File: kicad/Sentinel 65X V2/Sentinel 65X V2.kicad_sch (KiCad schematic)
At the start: 158 parts, among them J1 SNES Controller, J10 Conn_02x15_Counter_Clockwise, J11 Conn_01x02, J12 Conn_01x02, J13 LEFT, J14 RIGHT, J15 USB_C_Receptacle_PowerOnly_6P, J2 SNES Controller, J4 JTAG Header, J5 2x32 2.54mm Card Edge Connect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

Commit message: Updated pinouts
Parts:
- removed J10: Conn_02x15_Counter_Clockwise, symbol Sentinel 65X V2:Conn_02x15_Counter_Clockwise
- removed R81: 3.3kΩ, Resistor_SMD:R_0402_1005Metric, symbol Sentinel 65X V2:R
- added J10: FPGA Flash Prog, symbol Connector_Generic:Conn_02x04_Odd_Even
- added J3: Conn_02x12_Odd_Even, symbol Connector_Generic:Conn_02x12_Odd_Even
- added R44, R52, R60, R61: 10kΩ, Resistor_SMD:R_0402_1005Metric, symbol Sentinel 65X V2:R
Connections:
- net +3.3V: now also J3.2 (Pin_2), R44.1, R52.1, R60.1
- net A0: now also J3.16 (Pin_16)
- net A1: now also J3.15 (Pin_15)
- net A2: now also J3.14 (Pin_14)
- net A3: now also J3.13 (Pin_13)
- net CDONE: now also J10.1 (Pin_1)
- net D0: now also J3.24 (Pin_24)
- net D1: now also J3.23 (Pin_23)
- net D2: now also J3.22 (Pin_22)
- net D3: now also J3.21 (Pin_21)
- net D4: now also J3.20 (Pin_20)
- net D5: now also J3.19 (Pin_19)
- net D6: now also J3.18 (Pin_18)
- net D7: now also J3.17 (Pin_17)
- net FPGA_MISO: now also J10.6 (Pin_6), R60.2
- net FPGA_MOSI: now also J10.5 (Pin_5), R52.2
- net FPGA_SCK: now also J10.4 (Pin_4), R61.1
- net GND: now also J10.7 (Pin_7), J10.8 (Pin_8), J3.1 (Pin_1), R61.2
- net I2C_SCL: now also J3.4 (Pin_4)
- net I2C_SDA: now also J3.6 (Pin_6)
- net PHI2: now also J3.9 (Pin_9)
- net RXD: now also J3.5 (Pin_5)
- net TXD: now also J3.3 (Pin_3)
- net ~{CLOCK}: now also J3.10 (Pin_10)
- net ~{FLASH_SS}: now also J10.2 (Pin_2)
- net ~{FPGA_RES}: now also J10.3 (Pin_3), R44.2
- net ~{IRQ}2: now also J3.8 (Pin_8)
- net ~{RD}: now also J3.11 (Pin_11)
- net ~{RES}: now also J3.7 (Pin_7)
- net ~{WR}: now also J3.12 (Pin_12)
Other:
- moved on the sheet: R21, R70, R71

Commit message: Updated schematic to add RTS/CTS flow control to debug UART (required by CPU's on-chip ROM monitor)
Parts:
- removed J3: Conn_02x12_Odd_Even, symbol Connector_Generic:Conn_02x12_Odd_Even
- removed R38, R46, R70, R71: 3.3kΩ, Resistor_SMD:R_0402_1005Metric, symbol Sentinel 65X V2:R
- added D9: LED, symbol Sentinel 65X V2:LED
- added J3: Conn_02x13_Counter_Clockwise, symbol Connector_Generic:Conn_02x13_Counter_Clockwise
- R35: value 3.3kΩ -> 1kΩ
- U2: footprint Package_LCC:PLCC-84_SMD-Socket -> Package_LCC:PLCC-84_THT-Socket
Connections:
- net +3.3V: now also J3.26 (Pin_26); no longer R35.1
- net A0: now also J3.18 (Pin_18)
- net A1: now also J3.9 (Pin_9)
- net A2: now also J3.19 (Pin_19)
- net A3: now also J3.8 (Pin_8)
- net BL0: now also U2.4 (P60); no longer U2.77 (P47)
- net BL1: now also U2.5 (P61); no longer U2.76 (P46)
- net CDONE: now also R35.2; no longer R41.2
- net D0: now also J3.14 (Pin_14)
- net D1: now also J3.13 (Pin_13)
- net D2: now also J3.15 (Pin_15)
- net D3: now also J3.12 (Pin_12)
- net D4: now also J3.16 (Pin_16)
- net D5: now also J3.11 (Pin_11)
- net D6: now also J3.17 (Pin_17)
- net D7: now also J3.10 (Pin_10)
- net GND: now also D9.1 (K), J3.1 (Pin_1)
- net I2C_SCL: now also U2.77 (P47), J3.25 (Pin_25); no longer U2.11 (P67)
- net I2C_SDA: now also U2.76 (P46), J3.24 (Pin_24); no longer U2.9 (P65)
- net PHI2: now also J3.6 (Pin_6)
- net RXD: now also U2.9 (P65), J3.3 (Pin_3); no longer U2.6 (P62)
- net TXD: now also U2.11 (P67), J3.2 (Pin_2); no longer U2.5 (P61)
- net ~{CLOCK}: now also J3.21 (Pin_21)
- net ~{NMI}: now also J5.a26 (Pin_a26); no longer J5.b26 (Pin_b26)
- net ~{RD}: now also J3.7 (Pin_7)
- net ~{RES}: now also J3.23 (Pin_23)
- net ~{WR}: now also J3.20 (Pin_20)
- net IRQ3: no longer names the net of U4.5 (I/O/PD1)
- net IRQ3: no longer U2.4 (PE60)
- removed net VIRQ: J5.a26 (Pin_a26), U2.2 (PE56), U9.3 (IOB_9b)
- net ~{IRQ}0 renamed ~{IRQ}
- net ~{IRQ}: now also J3.22 (Pin_22)
- net ~{IRQ}2 renamed ~{VIRQ}
- net ~{VIRQ}: now also J5.a25 (Pin_a25), U2.8 (~{NE64}), U9.3 (IOB_9b); no longer U2.3 (~{NE57})
- removed net ~{IRQ}3: J5.b24 (Pin_b24), R35.2, U4.35 (I/O/GCLK3)
- net ~{IRQ}4: no longer names the net of J5.b25 (Pin_b25)
- net ~{IRQ}4: no longer U2.8 (~{NE64})
- removed net ~{IRQ}5: J5.a25 (Pin_a25), U2.10 (~{NE66})
- new net: D9.2 (A), R35.1
- new net BL2: R41.2, U2.6 (P62)
- new net CTS: J3.4 (Pin_4), U2.3 (P57)
- new net RTS: J3.5 (Pin_5), U2.2 (P56)
- no-connect marks 26 -> 31
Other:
- note added: "Clock OTP ROM Defaults: CLK: 32.768KHz TOD clock FCLK: 4MHz fast clock SYSCLK: 25MHz VERA clock"
- note removed: "Clock Defaults: CLK: 32.768KHz TOD clock FCLK: 8MHz+ fast clock SYSCLK: 25MHz VERA clock"
- moved on the sheet: D3, D4, D8, H1, H2, H3, H4, H5, H6, J12, J7, R23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

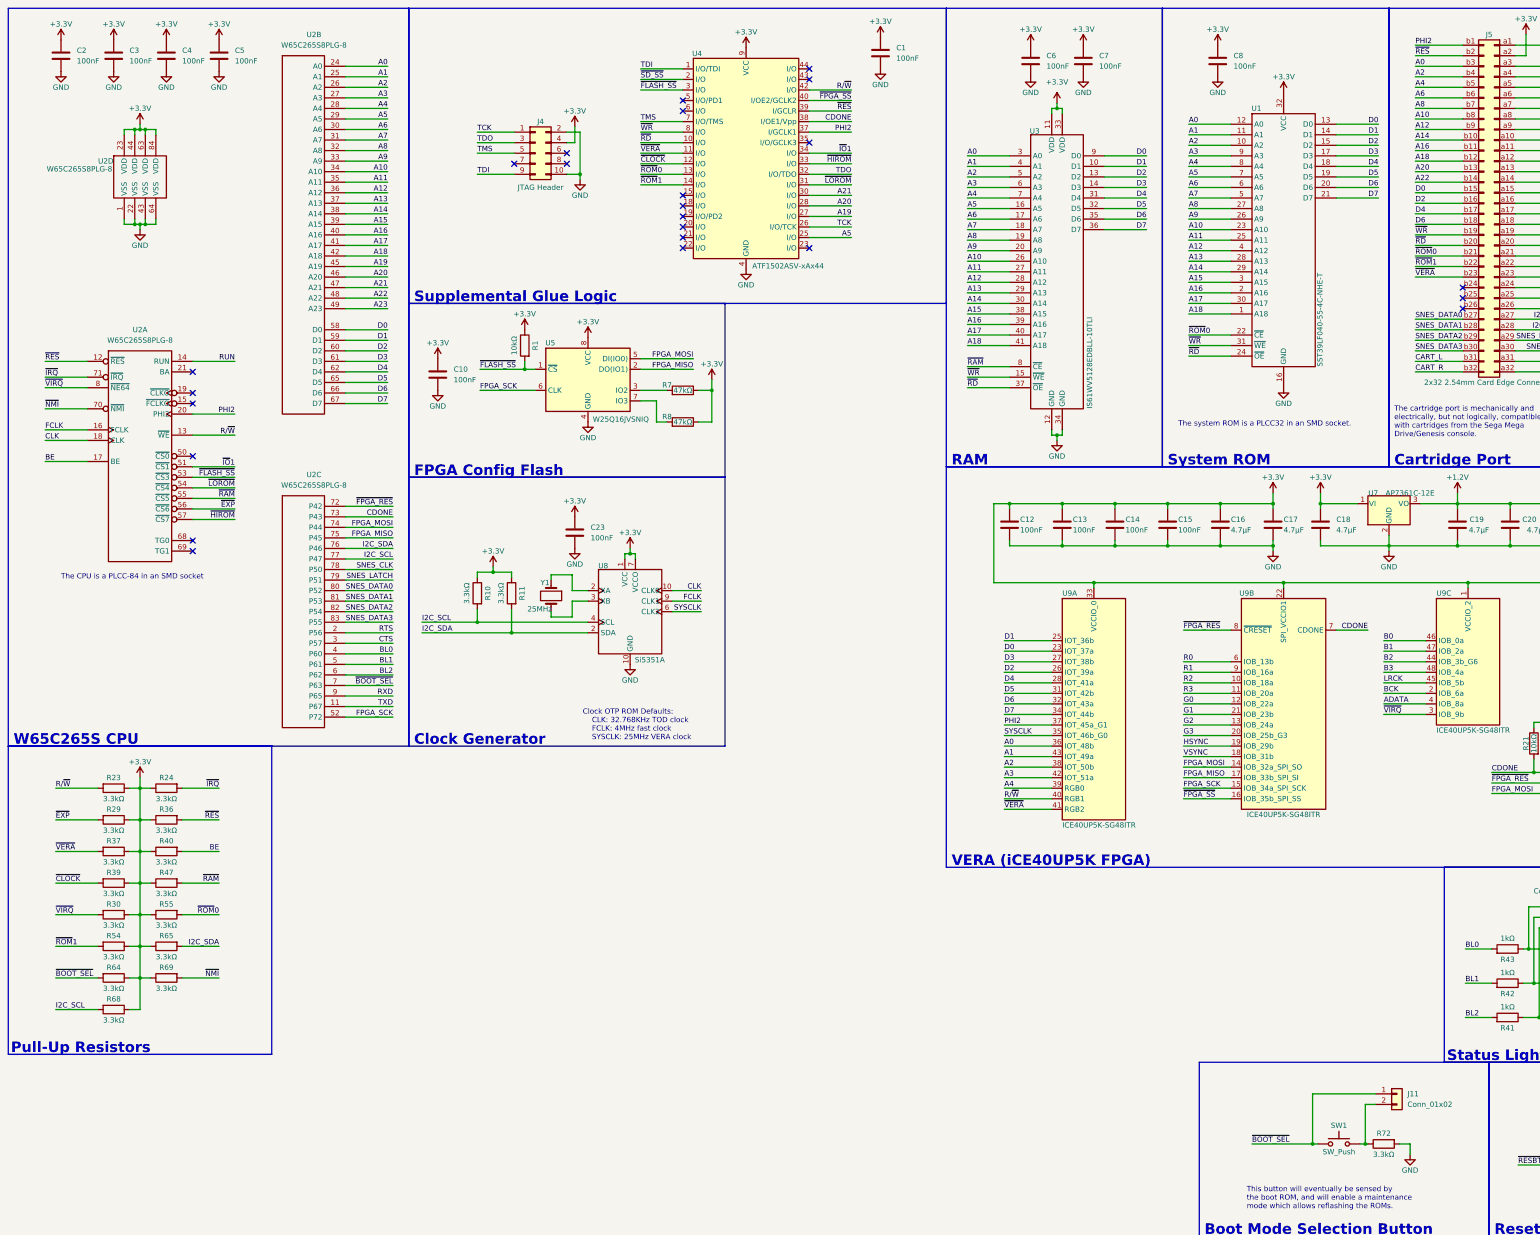
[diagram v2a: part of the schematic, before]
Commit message: Added version 3 and 4 prototype schematics
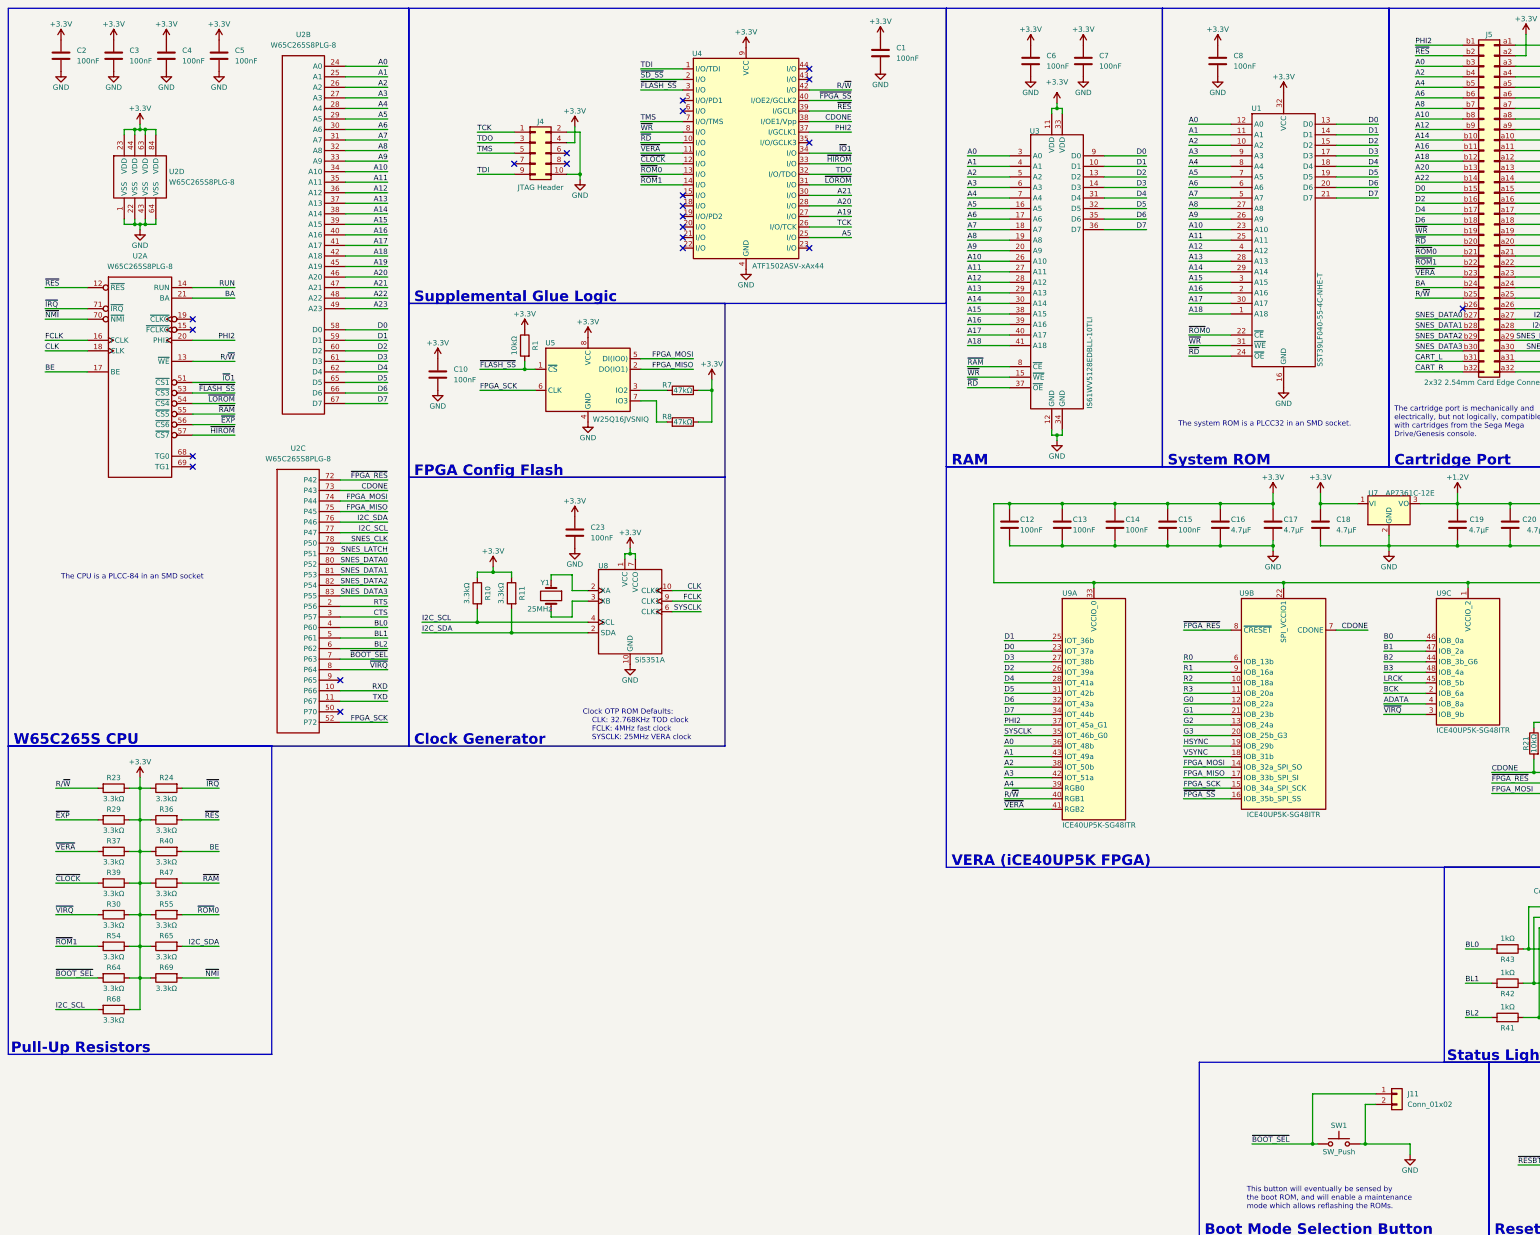
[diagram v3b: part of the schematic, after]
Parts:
- removed R72: 3.3kΩ, Resistor_SMD:R_0402_1005Metric, symbol Sentinel 65X V2:R
- removed U2: W65C265S8PLG-8, Package_LCC:PLCC-84_THT-Socket, symbol Sentinel 65X V2:W65C265S8PLG-8
- added U2: W65C265S8PLG-8, Package_LCC:PLCC-84_THT-Socket, symbol Western Design Center:W65C265S8PLG-8
- C24, C25, C27, C29, C30, C31: footprint (none) -> Capacitor_SMD:C_1206_3216Metric
- C38, C39: footprint (none) -> Capacitor_SMD:CP_Elec_6.3x5.4
- D3, D4, D8, D9: footprint (none) -> LED_SMD:LED_0603_1608Metric
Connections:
- net +3.3V: now also U2.23 (VDD), U2.44 (VDD), U2.63 (VDD), U2.84 (VDD)
- net A0: now also U2.24 (A0)
- net A1: now also U2.25 (A1)
- net A10: now also U2.34 (A10)
- net A11: now also U2.35 (A11)
- net A12: now also U2.36 (A12)
- net A13: now also U2.37 (A13)
- net A14: now also U2.38 (A14)
- net A15: now also U2.39 (A15)
- net A16: now also U2.40 (A16)
- net A17: now also U2.41 (A17)
- net A18: now also U2.42 (A18)
- net A19: now also U2.45 (A19)
- net A2: now also U2.26 (A2)
- net A20: now also U2.46 (A20)
- net A21: now also U2.47 (A21)
- net A22: now also U2.48 (A22)
- net A23: now also U2.49 (A23)
- net A3: now also U2.27 (A3)
- net A4: now also U2.28 (A4)
- net A5: now also U2.29 (A5)
- net A6: now also U2.30 (A6)
- net A7: now also U2.31 (A7)
- net A8: now also U2.32 (A8)
- net A9: now also U2.33 (A9)
- net BE: now also U2.17 (BE)
- net BL0: now also U2.4 (P60)
- net BL1: now also U2.5 (P61)
- net BL2: now also U2.6 (P62)
- net CDONE: now also U2.73 (P43)
- net CLK: now also U2.18 (CLK)
- net CTS: now also U2.3 (P57)
- net D0: now also U2.58 (D0)
- net D1: now also U2.59 (D1)
- net D2: now also U2.60 (D2)
- net D3: now also U2.61 (D3)
- net D4: now also U2.62 (D4)
- net D5: now also U2.65 (D5)
- net D6: now also U2.66 (D6)
- net D7: now also U2.67 (D7)
- net FCLK: now also U2.16 (FCLK)
- net FPGA_MISO: now also U2.75 (P45)
- net FPGA_MOSI: now also U2.74 (P44)
- net FPGA_SCK: now also U2.52 (P72)
- net GND: now also J11.2 (Pin_2), SW1.2, U2.1 (VSS), U2.22 (VSS), U2.43 (VSS), U2.64 (VSS)
- net I2C_SCL: now also U2.77 (P47)
- net I2C_SDA: now also U2.76 (P46)
- net PHI2: now also U2.20 (PHI2)
- net RTS: now also U2.2 (P56)
- net RUN: now also U2.14 (RUN)
- net RXD: now also U2.10 (P66)
- net R/~{W}: now also J5.b25 (Pin_b25), U2.13 (~{WE})
- net SNES_CLK: now also U2.78 (P50)
- net SNES_DATA0: now also U2.80 (P52)
- net SNES_DATA1: now also U2.81 (P53)
- net SNES_DATA2: now also U2.82 (P54)
- net SNES_DATA3: now also U2.83 (P55)
- net SNES_LATCH: now also U2.79 (P51)
- net TXD: now also U2.11 (P67)
- net ~{BOOT_SEL}: now also U2.7 (P63)
- net ~{EXP}: now also U2.56 (~{CS6})
- net ~{FLASH_SS}: now also U2.53 (~{CS3})
- net ~{FPGA_RES}: now also U2.72 (P42)
- net ~{HIROM}: now also U2.57 (~{CS7})
- net ~{IO}1: now also U2.51 (~{CS1})
- net ~{IRQ}: now also U2.71 (~{IRQ})
- net ~{LOROM}: now also U2.54 (~{CS4})
- net ~{NMI}: now also U2.70 (~{NMI})
- net ~{RAM}: now also U2.55 (~{CS5})
- net ~{RES}: now also U2.12 (~{RES})
- net ~{VIRQ}: now also U2.8 (P64)
- net BA: now reaches J5.b24 (Pin_b24)
- net BA: now also U2.21 (BA)
- no-connect marks 31 -> 29
